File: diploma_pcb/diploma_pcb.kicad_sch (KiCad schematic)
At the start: 15 parts, among them Q1 2SC3356, Q3 2SC3356

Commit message: asdasd
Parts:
- renumbered RData to RData1, R_gnd to R_gnd1, Rcc to Rcc1
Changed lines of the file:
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@@
 		(on_board yes)
 		(dnp no)
-		(property "Reference" "Rcc"
+		(property "Reference" "Rcc1"
 			(at 74.295 18.415 90)
 			(effects
@@
 			(project "diploma_pcb"
 				(path "/8eade999-89f4-4618-aeea-e9238b0bd165"
-					(reference "Rcc")
+					(reference "Rcc1")
 					(unit 1)
 				)
@@
 		(on_board yes)
 		(dnp no)
-		(property "Reference" "RData"
+		(property "Reference" "RData1"
 			(at 58.42 34.925 90)
 			(effects
@@
 			(project "diploma_pcb"
 				(path "/8eade999-89f4-4618-aeea-e9238b0bd165"
-					(reference "RData")
+					(reference "RData1")
 					(unit 1)
 				)
@@
 		(on_board yes)
 		(dnp no)
-		(property "Reference" "R_gnd"
+		(property "Reference" "R_gnd1"
 			(at 74.295 70.485 90)
 			(effects
@@
 			(project "diploma_pcb"
 				(path "/8eade999-89f4-4618-aeea-e9238b0bd165"
-					(reference "R_gnd")
-					(unit 1)
-				)
+					(reference "R_gnd1")
+					(unit 1)
+				)

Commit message: with capacitors
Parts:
- added C1, C2, C3: .1uF, Capacitor_SMD:C_1206_3216Metric_Pad1.33x1.80mm_HandSolder, symbol Device:C
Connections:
- net at 5_pins_op_amp1.2 (VSS), 8_pin_op_amp1.4 (V-), A1.29 (GND)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: now also C1.1
- net at R1.2, R6.1, R7.1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: now also C1.2, C2.2, C3.2; no longer 5_pins_op_amp1.5 (VDD), 8_pin_op_amp1.7 (V+)
- new net: 5_pins_op_amp1.5 (VDD), C3.1
- new net: 8_pin_op_amp1.7 (V+), C2.1

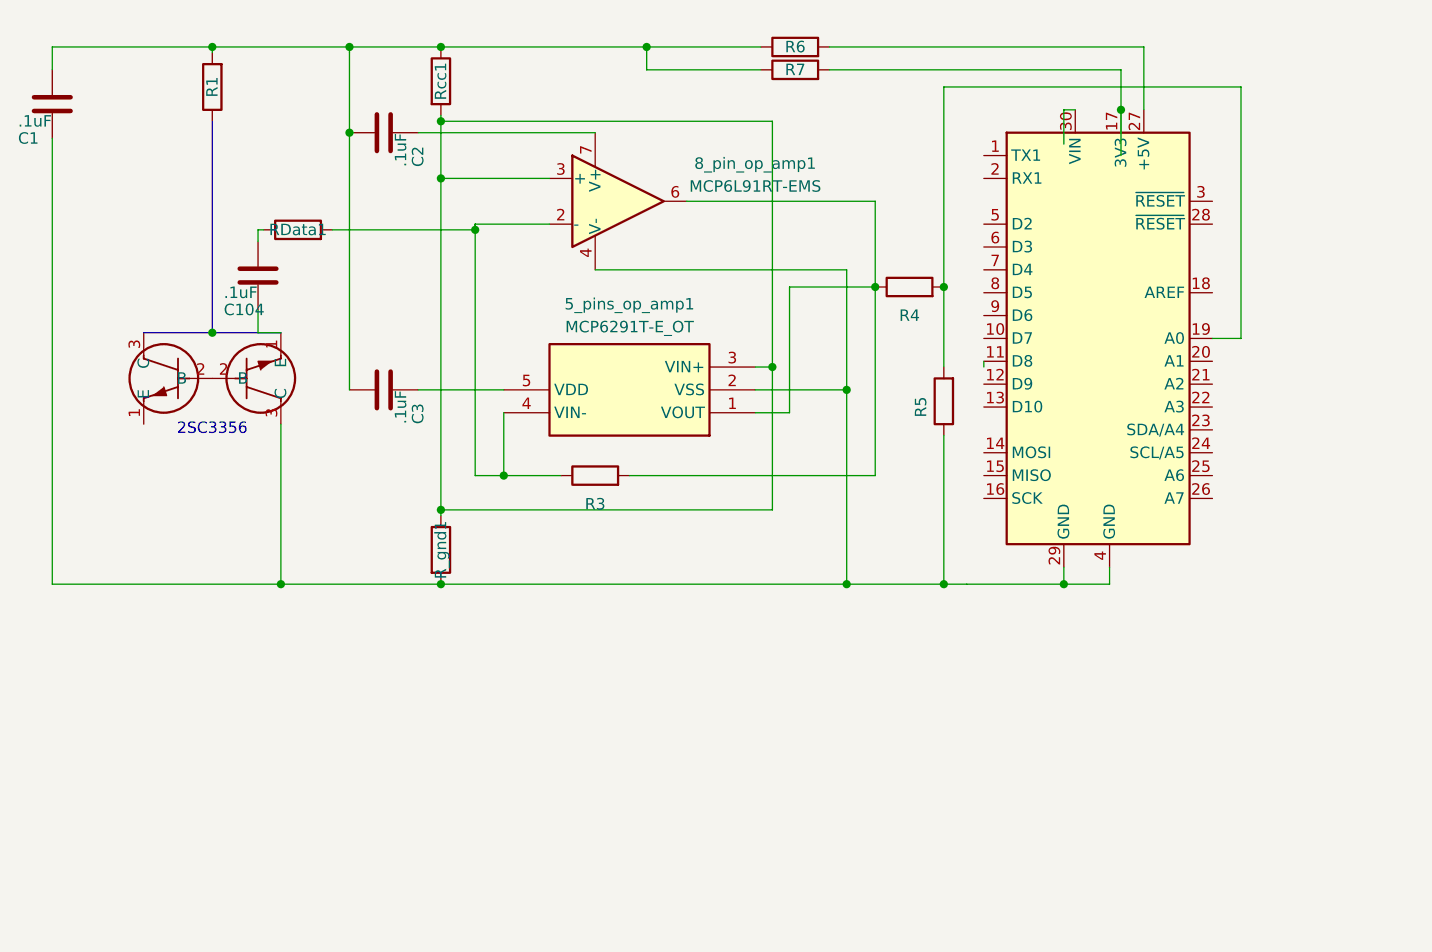
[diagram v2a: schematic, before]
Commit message: Fixed schematic with dimplomer
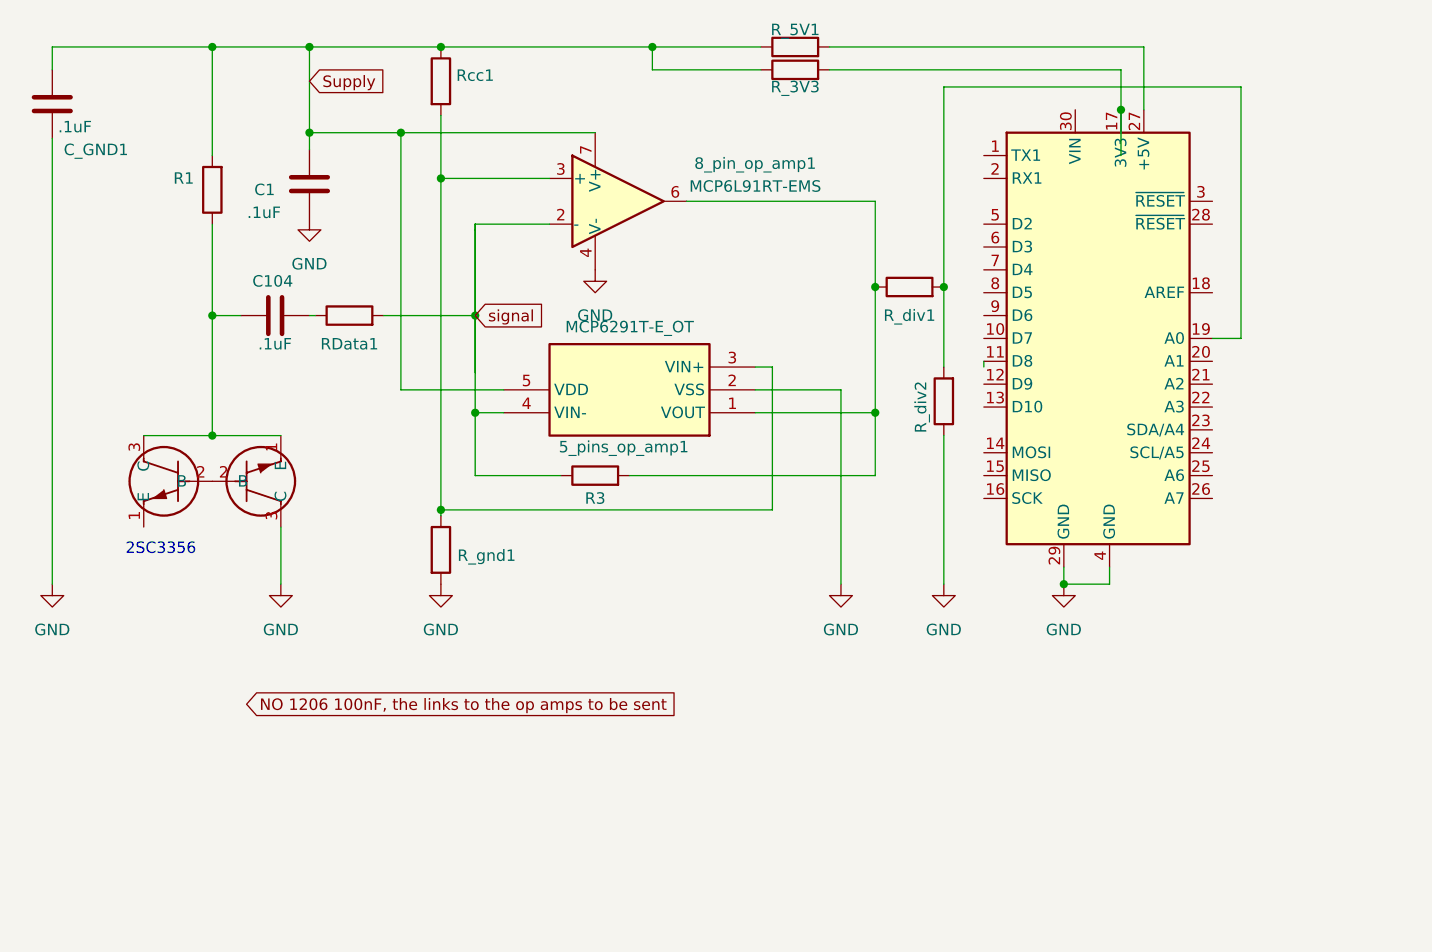
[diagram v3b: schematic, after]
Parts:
- removed C2, C3: .1uF, Capacitor_SMD:C_1206_3216Metric_Pad1.33x1.80mm_HandSolder, symbol Device:C
- added C1: .1uF, Capacitor_SMD:C_1206_3216Metric_Pad1.33x1.80mm_HandSolder, symbol Device:C
- renumbered C1 to C_GND1, R7 to R_3V3, R6 to R_5V1, R4 to R_div1, R5 to R_div2
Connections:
- net at C104.1, Q3.1 (E): now also Q1.3 (C), R1.1
- net GND: now reaches 5_pins_op_amp1.2 (VSS), 8_pin_op_amp1.4 (V-), A1.29 (GND), A1.4 (GND), C_GND1.1, Q3.3 (C), R_div2.1, R_gnd1.2
- net GND: now also C1.2
- net Supply: now reaches C_GND1.2, R1.2, R_3V3.1, R_5V1.1, Rcc1.1
- net Supply: now also 5_pins_op_amp1.5 (VDD), 8_pin_op_amp1.7 (V+), C1.1
- net signal: now reaches 5_pins_op_amp1.4 (VIN-), 8_pin_op_amp1.2 (-), R3.1, RData1.2
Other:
- moved on the sheet: C104, R1, RData1

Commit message: rgb placed
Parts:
- added LED1: MP008253, MP008253:MP008253, symbol MP008253:MP008253
- added R_LED_B1, R_LED_G1, R_LED_R1: R, Resistor_SMD:R_1206_3216Metric, symbol Device:R
- R1, R3, RData1, R_3V3, R_5V1, R_div1, R_div2, R_gnd1, Rcc1: footprint 1206:RESC3116X65N -> Resistor_SMD:R_1206_3216Metric
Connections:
- net GND: now also LED1.1 (K_RED), LED1.3 (K_GREEN), LED1.5 (K_BLUE)
- net at A1.11 (D8): now also R_LED_B1.1
- net at A1.12 (D9): now also R_LED_G1.1
- net at A1.13 (D10): now also R_LED_R1.1
- new net: LED1.2 (A_RED), R_LED_R1.2
- new net: LED1.4 (A_GREEN), R_LED_G1.2
- new net: LED1.6 (A_BLUE), R_LED_B1.2

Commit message: Working Serial Comunication!
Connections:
- net red: now reaches LED1.2 (A_RED), R_LED_R1.2
- net Vout: now reaches 5_pins_op_amp1.1 (VOUT), 8_pin_op_amp1.6, R3.2, R_div1.1
- net green: now reaches LED1.4 (A_GREEN), R_LED_G1.2
- net blue: now reaches LED1.6 (A_BLUE), R_LED_B1.2
- net 3.3V: now reaches A1.17 (3V3), R_3V3.2
- net 5V: now reaches A1.27 (+5V), R_5V1.2
- net non inv: now reaches 5_pins_op_amp1.3 (VIN+), 8_pin_op_amp1.3 (+), R_gnd1.1, Rcc1.2

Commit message: changes on schematic
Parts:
- added C2: .1uF, Capacitor_SMD:C_1206_3216Metric_Pad1.33x1.80mm_HandSolder, symbol Device:C
- R1: value R -> 1K
- R_gnd1, Rcc1: value R -> 3k
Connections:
- net GND: now also C2.2
- net non inv: now also C2.1
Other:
- moved on the sheet: C1
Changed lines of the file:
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@@
 	)
 	(junction
+		(at 85.09 66.04)
+		(diameter 0)
+		(color 0 0 0 0)
+	)
+	(junction
 		(at 74.295 29.21)
 		(diameter 0)
@@
 	(wire
 		(pts
+			(xy 85.09 66.04) (xy 111.125 66.04)
+		)
+		(stroke
+			(width 0)
+			(type default)
+			(color 0 0 255 1)
+		)
+	)
+	(wire
+		(pts
 			(xy 97.79 14.605) (xy 109.855 14.605)
 		)
@@
 	(wire
 		(pts
-			(xy 74.295 66.04) (xy 111.125 66.04)
+			(xy 74.295 66.04) (xy 85.09 66.04)
 		)
 		(stroke
@@
 	(wire
 		(pts
-			(xy 59.69 24.13) (xy 59.69 26.035)
+			(xy 59.69 24.13) (xy 59.69 26.67)
 		)
 		(stroke
@@
 	(symbol
 		(lib_id "power:GND")
-		(at 59.69 33.655 0)
+		(at 59.69 34.29 0)
 		(unit 1)
 		(exclude_from_sim no)
@@
 		(fields_autoplaced yes)
 		(property "Reference" "#PWR011"
-			(at 59.69 40.005 0)
+			(at 59.69 40.64 0)
 			(effects
 				(font
@@
 		)
 		(property "Value" "GND"
-			(at 59.69 38.735 0)
+			(at 59.69 39.37 0)
 			(effects
 				(font
@@
 		)
 		(property "Footprint" ""
-			(at 59.69 33.655 0)
+			(at 59.69 34.29 0)
 			(effects
 				(font
@@
 		)
 		(property "Datasheet" ""
-			(at 59.69 33.655 0)
+			(at 59.69 34.29 0)
 			(effects
 				(font
@@
 		)
 		(property "Description" "Power symbol creates a global label with name \"GND\" , ground"
-			(at 59.69 33.655 0)
+			(at 59.69 34.29 0)
 			(effects
 				(font
@@
 			)
 		)
-		(property "Value" "R"
-			(at 78.105 18.415 90)
+		(property "Value" "3k"
+			(at 77.978 19.812 0)
 			(effects
 				(font
 					(size 1.27 1.27)
 				)
-				(hide yes)
 			)
 		)
@@
 	)
 	(symbol
+		(lib_id "Device:C")
+		(at 85.09 69.85 0)
+		(mirror y)
+		(unit 1)
+		(exclude_from_sim no)
+		(in_bom yes)
+		(on_board yes)
+		(dnp no)
+		(property "Reference" "C2"
+			(at 88.9 70.485 0)
+			(effects
+				(font
+					(size 1.27 1.27)
+				)
+				(justify right)
+			)
+		)
+		(property "Value" ".1uF"
+			(at 88.265 73.025 0)
+			(effects
+				(font
+					(size 1.27 1.27)
+				)
+				(justify right)
+			)
+		)
+		(property "Footprint" "Capacitor_SMD:C_1206_3216Metric_Pad1.33x1.80mm_HandSolder"
+			(at 84.1248 73.66 0)
+			(effects
+				(font
+					(size 1.27 1.27)
+				)
+				(hide yes)
+			)
+		)
+		(property "Datasheet" "~"
+			(at 85.09 69.85 0)
+			(effects
+				(font
+					(size 1.27 1.27)
+				)
+				(hide yes)
+			)
+		)
+		(property "Description" "Unpolarized capacitor"
+			(at 85.09 69.85 0)
+			(effects
+				(font
+					(size 1.27 1.27)
+				)
+				(hide yes)
+			)
+		)
+		(pin "1"
+		)
+		(pin "2"
+		)
+		(instances
+			(project "diploma_pcb"
+				(path "/8eade999-89f4-4618-aeea-e9238b0bd165"
+					(reference "C2")
+					(unit 1)
+				)
+			)
+		)
+	)
+	(symbol
+		(lib_id "power:GND")
+		(at 85.09 73.66 0)
+		(unit 1)
+		(exclude_from_sim no)
+		(in_bom yes)
+		(on_board yes)
+		(dnp no)
+		(fields_autoplaced yes)
+		(property "Reference" "#PWR012"
+			(at 85.09 80.01 0)
+			(effects
+				(font
+					(size 1.27 1.27)
+				)
+				(hide yes)
+			)
+		)
+		(property "Value" "GND"
+			(at 85.09 78.74 0)
+			(effects
+				(font
+					(size 1.27 1.27)
+				)
+			)
+		)
+		(property "Footprint" ""
+			(at 85.09 73.66 0)
+			(effects
+				(font
+					(size 1.27 1.27)
+				)
+				(hide yes)
+			)
+		)
+		(property "Datasheet" ""
+			(at 85.09 73.66 0)
+			(effects
+				(font
+					(size 1.27 1.27)
+				)
+				(hide yes)
+			)
+		)
+		(property "Description" "Power symbol creates a global label with name \"GND\" , ground"
+			(at 85.09 73.66 0)
+			(effects
+				(font
+					(size 1.27 1.27)
+				)
+				(hide yes)
+			)
+		)
+		(pin "1"
+		)
+		(instances
+			(project "diploma_pcb"
+				(path "/8eade999-89f4-4618-aeea-e9238b0bd165"
+					(reference "#PWR012")
+					(unit 1)
+				)
+			)
+		)
+	)
+	(symbol
 		(lib_id "power:GND")
 		(at 56.515 74.295 0)
@@
 	(symbol
 		(lib_id "Device:C")
-		(at 59.69 29.845 0)
+		(at 59.69 30.48 0)
 		(mirror y)
 		(unit 1)
@@
 		(dnp no)
 		(property "Reference" "C1"
-			(at 63.5 30.48 0)
+			(at 63.5 31.115 0)
 			(effects
 				(font
@@
 		)
 		(property "Value" ".1uF"
-			(at 62.865 33.02 0)
+			(at 62.865 33.655 0)
 			(effects
 				(font
@@
 		)
 		(property "Footprint" "Capacitor_SMD:C_1206_3216Metric_Pad1.33x1.80mm_HandSolder"
-			(at 58.7248 33.655 0)
+			(at 58.7248 34.29 0)
 			(effects
 				(font
@@
 		)
 		(property "Datasheet" "~"
-			(at 59.69 29.845 0)
+			(at 59.69 30.48 0)
 			(effects
 				(font
@@
 		)
 		(property "Description" "Unpolarized capacitor"
-			(at 59.69 29.845 0)
+			(at 59.69 30.48 0)
 			(effects
 				(font
@@
 			)
 		)
-		(property "Value" "R"
-			(at 78.105 70.485 90)
+		(property "Value" "3k"
+			(at 78.994 74.168 0)
 			(effects
 				(font
 					(size 1.27 1.27)
 				)
-				(hide yes)
 			)
 		)
@@
 			)
 		)
-		(property "Value" "R"
-			(at 45.085 30.48 90)
+		(property "Value" "1K"
+			(at 45.72 31.242 0)
 			(effects
 				(font
 					(size 1.27 1.27)
 				)
-				(hide yes)
 			)
 		)

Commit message: PCB values chosen and set
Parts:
- R1: value 1K -> 510
- Rf: renamed from R3; value R -> 510к
- Rg: renamed from RData1; value R -> 15к
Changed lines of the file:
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@@
 		(on_board yes)
 		(dnp no)
-		(property "Reference" "R3"
+		(property "Reference" "Rf"
 			(at 91.44 64.77 90)
 			(effects
@@
 			)
 		)
-		(property "Value" "R"
-			(at 91.44 58.42 90)
-			(effects
-				(font
-					(size 1.27 1.27)
-				)
-				(hide yes)
+		(property "Value" "510к"
+			(at 91.694 62.23 90)
+			(effects
+				(font
+					(size 1.27 1.27)
+				)
 			)
 		)
@@
 			(project "diploma_pcb"
 				(path "/8eade999-89f4-4618-aeea-e9238b0bd165"
-					(reference "R3")
+					(reference "Rf")
 					(unit 1)
 				)
@@
 		(on_board yes)
 		(dnp no)
-		(property "Reference" "RData1"
+		(property "Reference" "Rg"
 			(at 64.135 47.625 90)
 			(effects
@@
 			)
 		)
-		(property "Value" "R"
-			(at 64.135 40.64 90)
-			(effects
-				(font
-					(size 1.27 1.27)
-				)
-				(hide yes)
+		(property "Value" "15к"
+			(at 64.008 44.45 90)
+			(effects
+				(font
+					(size 1.27 1.27)
+				)
 			)
 		)
@@
 			(project "diploma_pcb"
 				(path "/8eade999-89f4-4618-aeea-e9238b0bd165"
-					(reference "RData1")
+					(reference "Rg")
 					(unit 1)
 				)
@@
 			)
 		)
-		(property "Value" "1K"
+		(property "Value" "510"
 			(at 45.72 31.242 0)
 			(effects
